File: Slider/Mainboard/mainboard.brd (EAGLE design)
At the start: 100 x 160 mm, 60 parts, among them IC1 7805TV, IC2 33CV, IC3 LM358, Q1 16MHz, SW1 MS MOT1, SW2 MS MOT2, T1 BC337, T2 BC337, U1 ATMEGA328P_PDIP, U2 MAX232PTH

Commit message: Started layouting seperate modules
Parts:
- added D2: 1N4004, diode:DO41-10
- moved T2 218.8 mm to (129.5, 87.6)
- moved D1 169.4 mm to (132.1, 78.7), turned to 180 degrees
- moved R16 142.6 mm to (11.4, 59.7), turned to 90 degrees
- moved JP7 130.3 mm to (6.35, 72.4), turned to 270 degrees
- moved IC3 124.9 mm to (14.0, 72.4), turned to 270 degrees
- moved C13 113.2 mm to (67.3, 96.5)
- moved R14 112.6 mm to (6.35, 87.6), turned to 270 degrees
- moved R12 108.4 mm to (11.4, 87.6), turned to 270 degrees
- moved R15 104.4 mm to (16.5, 87.6), turned to 90 degrees
- moved R1 101.3 mm to (55.9, 94.0)
- moved R11 91.2 mm to (115.6, 81.3)
- moved C1 90.3 mm to (16.5, 14.0), turned to 90 degrees
- moved JP3 78.7 mm to (26.7, 153.7), turned to 0 degrees
- moved JP2 77.5 mm to (74.9, 152.4), turned to 0 degrees
- moved SW1 77.5 mm to (57.1, 139.7)
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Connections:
- new net N$41: D2.A, JP1.PWR
- net +24V: now also C7.+, C8.+, D2.C; no longer JP1.PWR
- net 5V: no longer C7.+, C8.+
- net RESET: now also U1.1
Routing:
- net 5V: track 0.00 -> 219.7 mm
- net GND: track 0.00 -> 190.3 mm
- net N$37: track 0.00 -> 97.4 mm
- net N$16: track 0.00 -> 45.8 mm
- net N$4: track 0.00 -> 44.5 mm
- net N$26: track 0.00 -> 40.4 mm
- net RESET: track 0.00 -> 35.9 mm
- net HOMING: track 0.00 -> 35.1 mm
- net +24V: track 0.00 -> 33.5 mm
- net RIGHT: track 0.00 -> 31.9 mm
- net LEFT: track 0.00 -> 30.7 mm
- net N$14: track 0.00 -> 27.0 mm
- net N$2: track 0.00 -> 25.7 mm
- net TILTCW: track 0.00 -> 22.0 mm
- net 3.3V: track 0.00 -> 21.9 mm
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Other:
- board size 100 x 160 mm -> 194 x 160 mm

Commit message: Further board layouting
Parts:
- R1, R10, R11, R12, R14, R15, R2, R3, R4, R5, R6, R7, R8, R9: device rcl:0411/15 -> rcl:0207/7
- moved R3 131.7 mm to (105.4, 19.1)
- moved R4 131.7 mm to (110.5, 19.1)
- moved JP6 126.7 mm to (108.0, 6.35)
- moved T1 126.7 mm to (108.0, 11.4)
- moved SW2 93.7 mm to (29.2, 48.3)
- moved SW1 91.7 mm to (63.5, 48.3)
- moved JP3 87.5 mm to (47.0, 68.6)
- moved C8 86.2 mm to (59.7, 59.7)
- moved U$2 86.2 mm to (47.0, 52.1)
- moved JP2 84.1 mm to (81.3, 68.6)
- moved C7 84.1 mm to (94.0, 59.7)
- moved U$1 84.1 mm to (81.3, 52.1)
- moved S1 64.8 mm to (26.7, 31.8), turned to 270 degrees
- moved JP5 61.6 mm to (57.1, 27.9), turned to 0 degrees
- moved R1 61.3 mm to (49.5, 33.0)
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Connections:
- removed net DIR: U$1.DIR, U$2.DIR, U1.11, U1.13
- removed net MOSI: JP5.4, U1.17
- removed net STEP: U$1.STEP, U$2.STEP, U1.12, U1.6
- new net DIR1: U$1.DIR, U1.24
- new net DIR2: U$2.DIR, U1.26
- new net STEP1: U$1.STEP, U1.25
- new net STEP2: U$2.STEP, U1.27
- net HOMING: now also JP5.4, U1.17; no longer U1.27
- net LEFT: now also U1.11; no longer U1.23
- net N$31: now also U1.14; no longer U1.15
- net N$38: now also U1.28; no longer U1.14
- net RIGHT: now also U1.13; no longer U1.24
- net RXD: now also U1.5; no longer U1.4
- net STATUS: now also U1.16; no longer U1.28
- net TILTCCW: now also U1.12; no longer U1.26
- net TILTCW: now also U1.15; no longer U1.25
- net TXD: now also U1.4; no longer U1.5
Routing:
- net RXD: track 0.00 -> 180.8 mm
- net TXD: track 1.27 -> 158.4 mm
- net HOMING: track 35.1 -> 124.2 mm
- net RIGHT: track 31.9 -> 114.3 mm
- net ESPRX: track 0.00 -> 77.9 mm
- net TILTCCW: track 17.0 -> 93.2 mm
- net TILTCW: track 22.0 -> 96.4 mm
- net LEFT: track 30.7 -> 98.5 mm
- net STATUS: track 0.00 -> 64.5 mm
- net ESPTX: track 0.00 -> 64.1 mm
- net N$37: track 97.4 -> 34.4 mm
- net STEP1: track 0.00 -> 60.8 mm
- net DIR1: track 0.00 -> 58.3 mm
- net N$31: track 0.00 -> 56.8 mm
- net N$38: track 8.67 -> 62.4 mm
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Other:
- board size 194 x 160 mm -> 144.4 x 74 mm

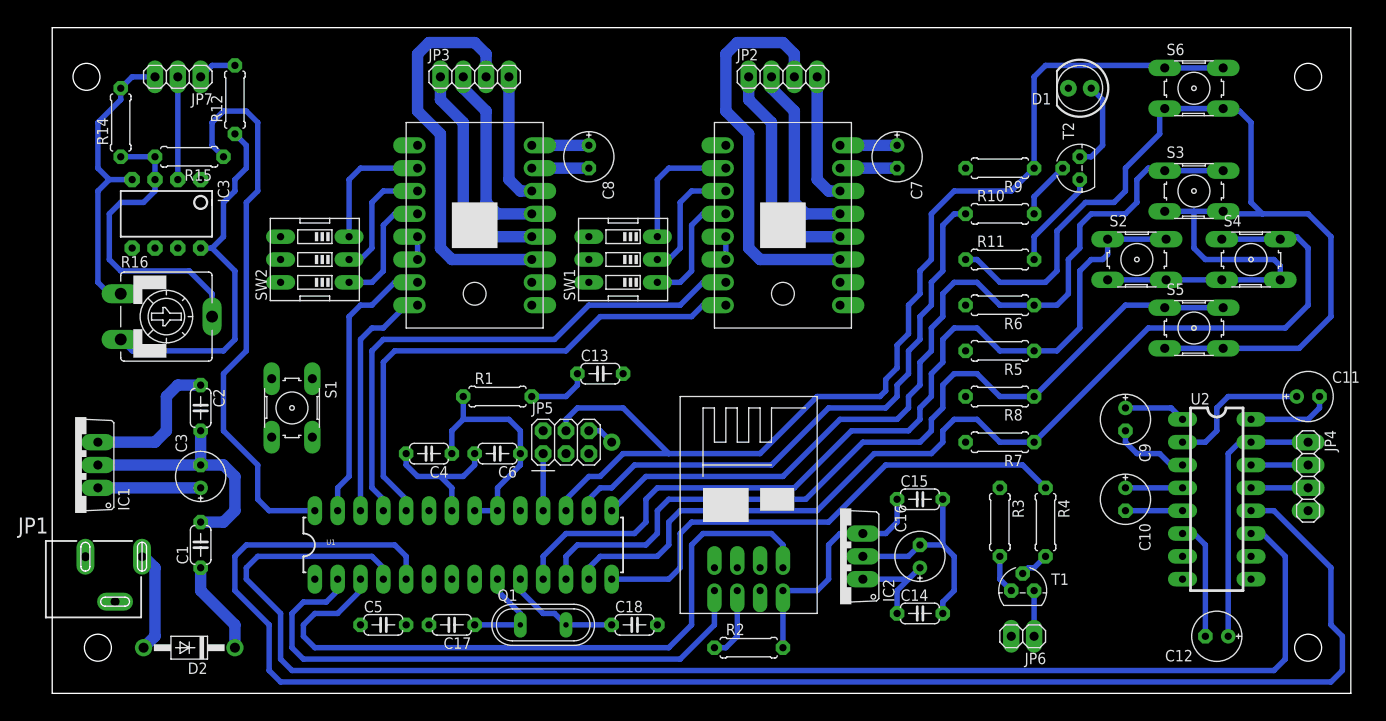
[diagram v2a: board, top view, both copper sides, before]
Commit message: progress in board layout and schematic
- fixed the layout of the schematic after pin swapping
- board connections all done
- board layout all done
- adjusted outline to match case
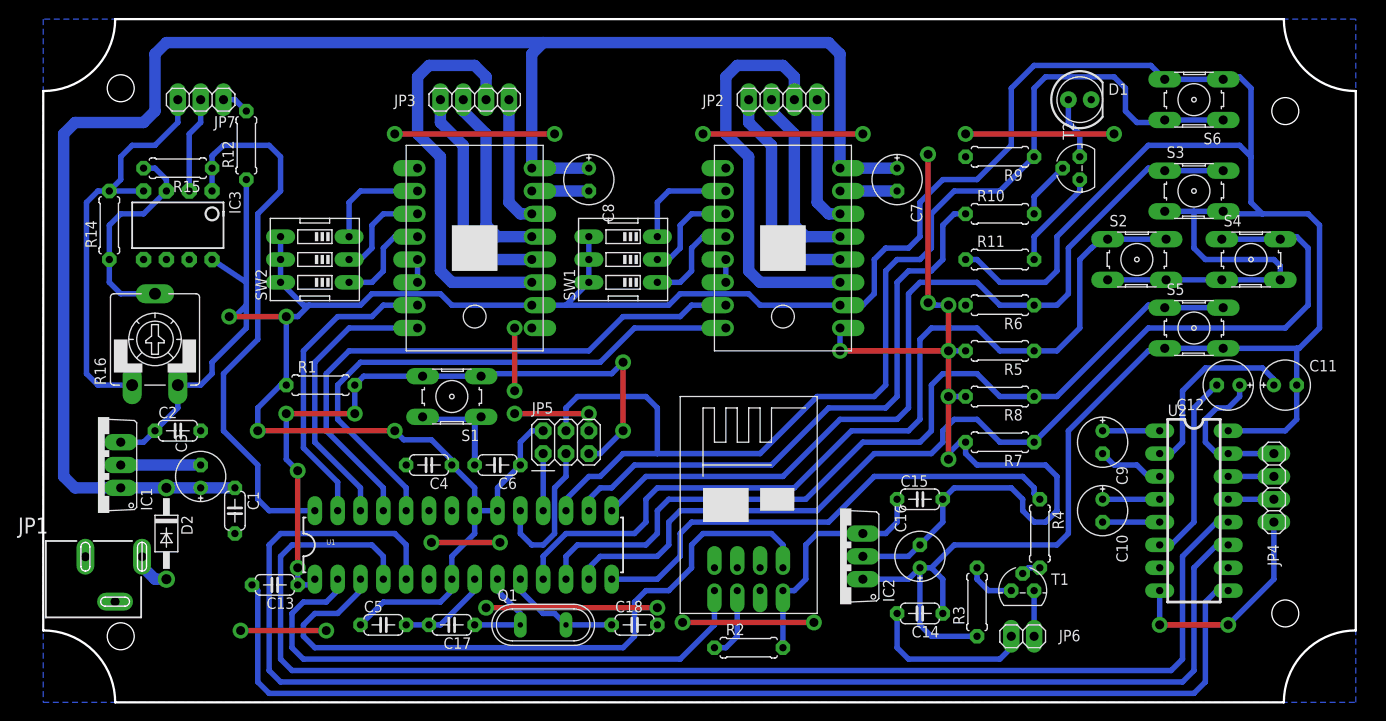
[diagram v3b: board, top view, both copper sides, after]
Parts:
- D1: value (none) -> STATUS
- JP1: value POWER_JACKSLT -> 12V IN
- moved C13 43.2 mm to (24.8, 12.1), turned to 180 degrees
- moved C12 28.0 mm to (130.8, 34.3)
- moved R1 19.7 mm to (29.8, 34.3)
- moved S1 17.8 mm to (44.5, 33.0), turned to 180 degrees
- moved D2 13.0 mm to (12.7, 17.8), turned to 270 degrees
- moved R14 11.5 mm to (6.35, 52.1)
- moved R3 9.25 mm to (102.9, 10.2), turned to 90 degrees
- moved C1 5.39 mm to (20.3, 20.3), turned to 270 degrees
- moved R12 5.24 mm to (21.6, 61.0)
- moved JP4 4.02 mm to (135.9, 22.9)
- moved C2 3.59 mm to (14.0, 29.2), turned to 0 degrees
- moved JP7 3.59 mm to (16.5, 66.0)
- moved C9 3.59 mm to (116.8, 27.9)
- moved R16 2.84 mm to (11.4, 39.4), turned to 0 degrees
- moved C10 2.84 mm to (116.8, 20.3)
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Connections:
- net 5V: now also SW1.4, SW1.5, SW1.6, SW2.4, SW2.5, SW2.6
- net RXD: now also U1.4; no longer U1.5
- net TXD: now also U1.5; no longer U1.4
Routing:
- net 5V: track 245.5 -> 504.6 mm, vias 0 -> 4
- net GND: track 145.6 -> 355.4 mm, vias 0 -> 25
- net +24V: track 34.6 -> 192.4 mm
- net N$10: track 0.00 -> 129.5 mm
- net RESET: track 6.88 -> 76.2 mm, vias 0 -> 6
- net RXD: track 180.8 -> 145.9 mm
- net N$26: track 0.00 -> 25.0 mm, vias 0 -> 2
- net SCK: track 0.00 -> 16.8 mm
- net N$37: track 34.4 -> 24.2 mm
- net N$25: track 13.2 -> 21.2 mm
- net N$41: track 11.4 -> 4.58 mm
- net HOMING: track 124.2 -> 130.5 mm
- net N$24: track 16.3 -> 21.2 mm
- net DIR2: track 27.0 -> 31.6 mm
- net DIR1: track 58.3 -> 62.9 mm
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- added copper zone on layer 16, net GND
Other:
- board size 144.4 x 74 mm -> 146 x 76 mm

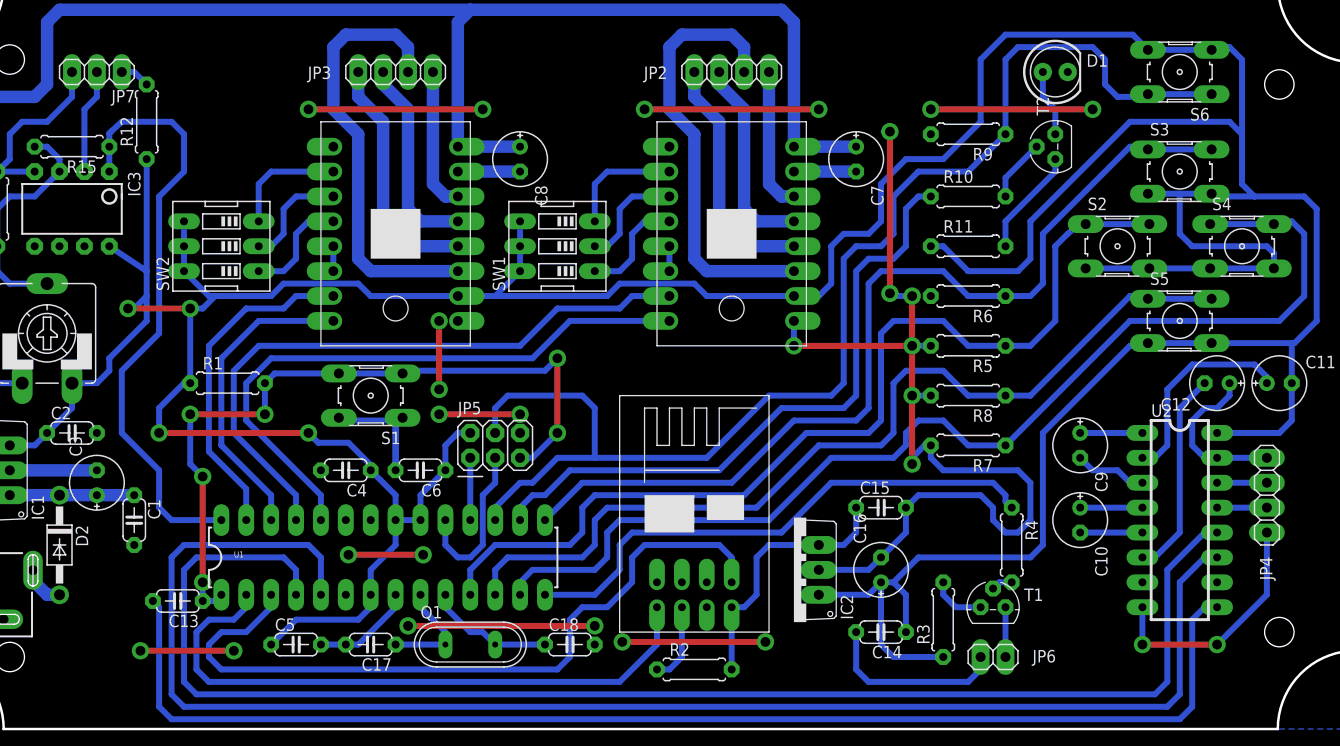
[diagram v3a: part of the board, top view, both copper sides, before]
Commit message: switched from generic pinheaders to the right connector footprint
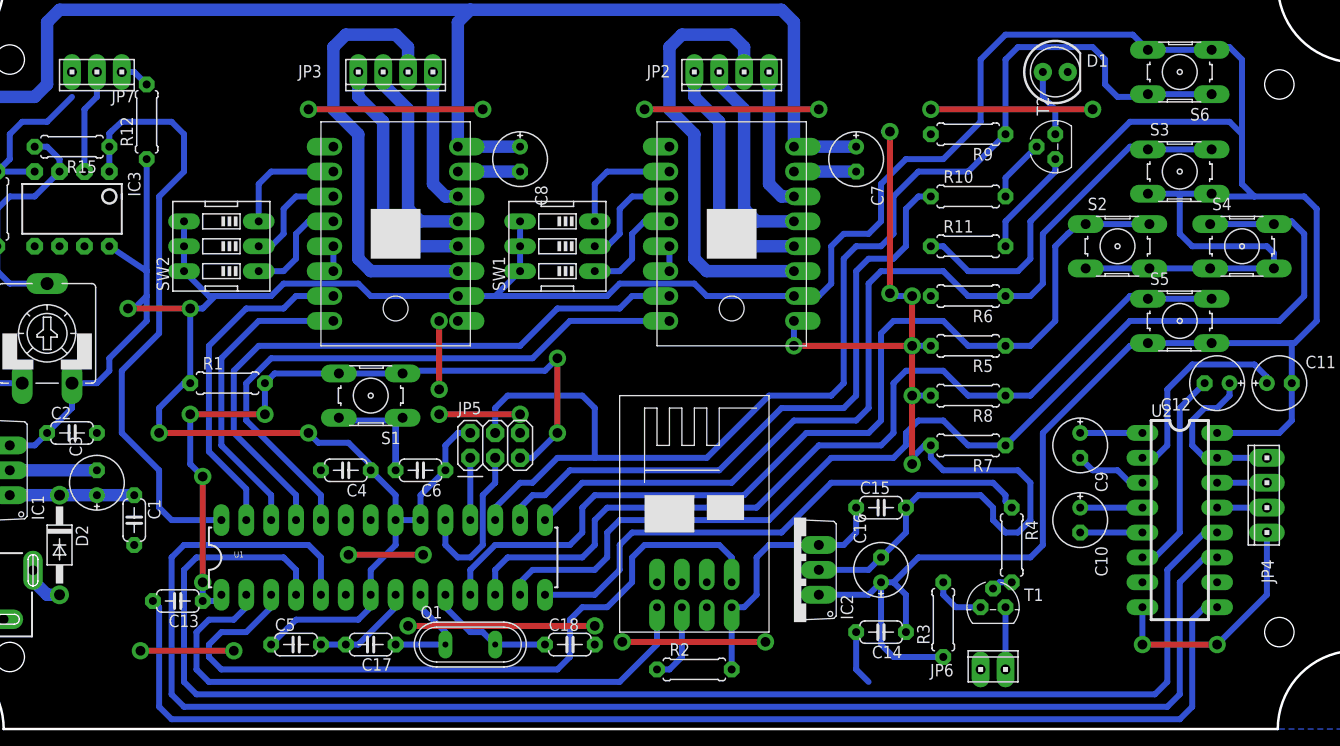
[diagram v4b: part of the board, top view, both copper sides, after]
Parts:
- JP2, JP3, JP4: device pinhead:1X04 -> con-amp:10X04MTA
- JP6: device pinhead:1X02 -> con-amp:10X02MTA
- JP7: device pinhead:1X03 -> con-amp:10X03MTA
- moved JP6 1.27 mm to (108.0, 5.08), turned to 0 degrees
- turned JP2 to 180 degrees
- turned JP3 to 180 degrees
- turned JP4 to 90 degrees
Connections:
- net GND: now also JP7.1; no longer JP7.3
- net N$35: now also JP7.3; no longer JP7.1
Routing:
- net GND: track 355.4 -> 339.6 mm
- net N$30: track 5.08 -> 6.35 mm
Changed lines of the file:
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@@
 <attribute name="VALUE" x="15.24" y="12.7" size="1.778" layer="27" rot="R90" align="top-center"/>
 </element>
-<element name="JP2" library="pinhead" package="1X04" value="MOT1" x="81.28" y="66.04" smashed="yes">
-<attribute name="NAME" x="72.3138" y="65.3288" size="1.27" layer="25" ratio="10"/>
+<element name="JP2" library="con-amp" package="10X04MTA" value="MOT1" x="81.28" y="66.04" smashed="yes" rot="R180">
+<attribute name="NAME" x="75.0062" y="66.7512" size="1.27" layer="25" ratio="10" rot="R180"/>
 <attribute name="VALUE" x="81.28" y="70.485" size="1.27" layer="27" align="top-center"/>
 </element>
-<element name="JP3" library="pinhead" package="1X04" value="MOT2" x="46.99" y="66.04" smashed="yes">
-<attribute name="NAME" x="38.0238" y="65.3288" size="1.27" layer="25" ratio="10"/>
+<element name="JP3" library="con-amp" package="10X04MTA" value="MOT2" x="46.99" y="66.04" smashed="yes" rot="R180">
+<attribute name="NAME" x="39.4462" y="66.7512" size="1.27" layer="25" ratio="10" rot="R180"/>
 <attribute name="VALUE" x="46.99" y="70.485" size="1.27" layer="27" align="top-center"/>
 </element>
-<element name="JP4" library="pinhead" package="1X04" value="RS232" x="135.89" y="22.86" smashed="yes" rot="R270">
-<attribute name="NAME" x="135.1788" y="16.5862" size="1.27" layer="25" ratio="10" rot="R270"/>
-<attribute name="VALUE" x="141.605" y="22.86" size="1.27" layer="27" rot="R270" align="top-center"/>
+<element name="JP4" library="con-amp" package="10X04MTA" value="RS232" x="135.89" y="22.86" smashed="yes" rot="R90">
+<attribute name="NAME" x="136.6012" y="13.8938" size="1.27" layer="25" ratio="10" rot="R90"/>
+<attribute name="VALUE" x="139.065" y="22.86" size="1.27" layer="27" rot="R90" align="top-center"/>
 </element>
 <element name="JP5" library="SparkFun-Connectors" package="2X03" value="ICSP" x="57.15" y="27.94"/>
-<element name="JP6" library="pinhead" package="1X02" value="IR" x="107.95" y="6.35" smashed="yes" rot="R180">
-<attribute name="NAME" x="114.3762" y="7.0612" size="1.27" layer="25" ratio="10" rot="R180"/>
-<attribute name="VALUE" x="107.95" y="1.905" size="1.27" layer="27" rot="R180" align="top-center"/>
-</element>
-<element name="JP7" library="pinhead" package="1X03" value="ENDSTOP" x="16.51" y="66.04" smashed="yes" rot="R180">
+<element name="JP6" library="con-amp" package="10X02MTA" value="IR" x="107.95" y="5.08" smashed="yes">
+<attribute name="NAME" x="101.5238" y="4.3688" size="1.27" layer="25" ratio="10"/>
+<attribute name="VALUE" x="107.95" y="9.525" size="1.27" layer="27" align="top-center"/>
+</element>
+<element name="JP7" library="con-amp" package="10X03MTA" value="ENDSTOP" x="16.51" y="66.04" smashed="yes" rot="R180">
 <attribute name="NAME" x="20.3962" y="64.2112" size="1.27" layer="25" ratio="10" rot="R180"/>
 <attribute name="VALUE" x="16.51" y="70.485" size="1.27" layer="27" rot="R180" align="bottom-center"/>
@@
 <contactref element="R7" pad="2"/>
 <contactref element="R9" pad="2"/>
-<contactref element="JP7" pad="3"/>
 <contactref element="IC3" pad="4"/>
 <contactref element="R14" pad="2"/>
@@
 <wire x1="93.98" y1="8.89" x2="93.98" y2="5.08" width="0.6096" layer="16"/>
 <wire x1="93.98" y1="5.08" x2="95.25" y2="3.81" width="0.6096" layer="16"/>
-<wire x1="95.25" y1="3.81" x2="105.41" y2="3.81" width="0.6096" layer="16"/>
-<wire x1="105.41" y1="3.81" x2="106.68" y2="5.08" width="0.6096" layer="16"/>
-<wire x1="106.68" y1="5.08" x2="106.68" y2="6.35" width="0.6096" layer="16"/>
 <wire x1="110.49" y1="25.4" x2="102.87" y2="25.4" width="0.6096" layer="16"/>
 <wire x1="3.81" y1="54.61" x2="5.08" y2="55.88" width="0.6096" layer="16"/>
@@
 <wire x1="8.89" y1="60.96" x2="11.43" y2="60.96" width="0.6096" layer="16"/>
 <wire x1="11.43" y1="60.96" x2="13.97" y2="63.5" width="0.6096" layer="16"/>
-<wire x1="13.97" y1="63.5" x2="13.97" y2="66.04" width="0.6096" layer="16"/>
 <wire x1="46.99" y1="11.43" x2="46.99" y2="12.7" width="0.6096" layer="16"/>
 <wire x1="46.99" y1="11.43" x2="43.18" y2="7.62" width="0.6096" layer="16"/>
@@
 <via x="118.11" y="62.23" extent="1-16" drill="1" diameter="1.778" shape="octagon"/>
 <wire x1="101.6" y1="62.23" x2="118.11" y2="62.23" width="0.6096" layer="1"/>
+<contactref element="JP7" pad="1"/>
 </signal>
 <signal name="5V">
@@
 <contactref element="T1" pad="1"/>
 <contactref element="JP6" pad="1"/>
-<wire x1="109.22" y1="11.43" x2="109.22" y2="6.35" width="0.6096" layer="16"/>
+<wire x1="109.22" y1="11.43" x2="109.22" y2="5.08" width="0.6096" layer="16"/>
 </signal>
 <signal name="LEFT">
@@
 <signal name="N$35">
 <contactref element="R12" pad="2"/>
-<contactref element="JP7" pad="1"/>
 <wire x1="21.59" y1="64.77" x2="20.32" y2="66.04" width="0.6096" layer="16"/>
+<contactref element="JP7" pad="3"/>
 <wire x1="20.32" y1="66.04" x2="19.05" y2="66.04" width="0.6096" layer="16"/>
 </signal>
